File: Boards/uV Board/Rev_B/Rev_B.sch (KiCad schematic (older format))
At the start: 3 parts, among them M2.5 CMH

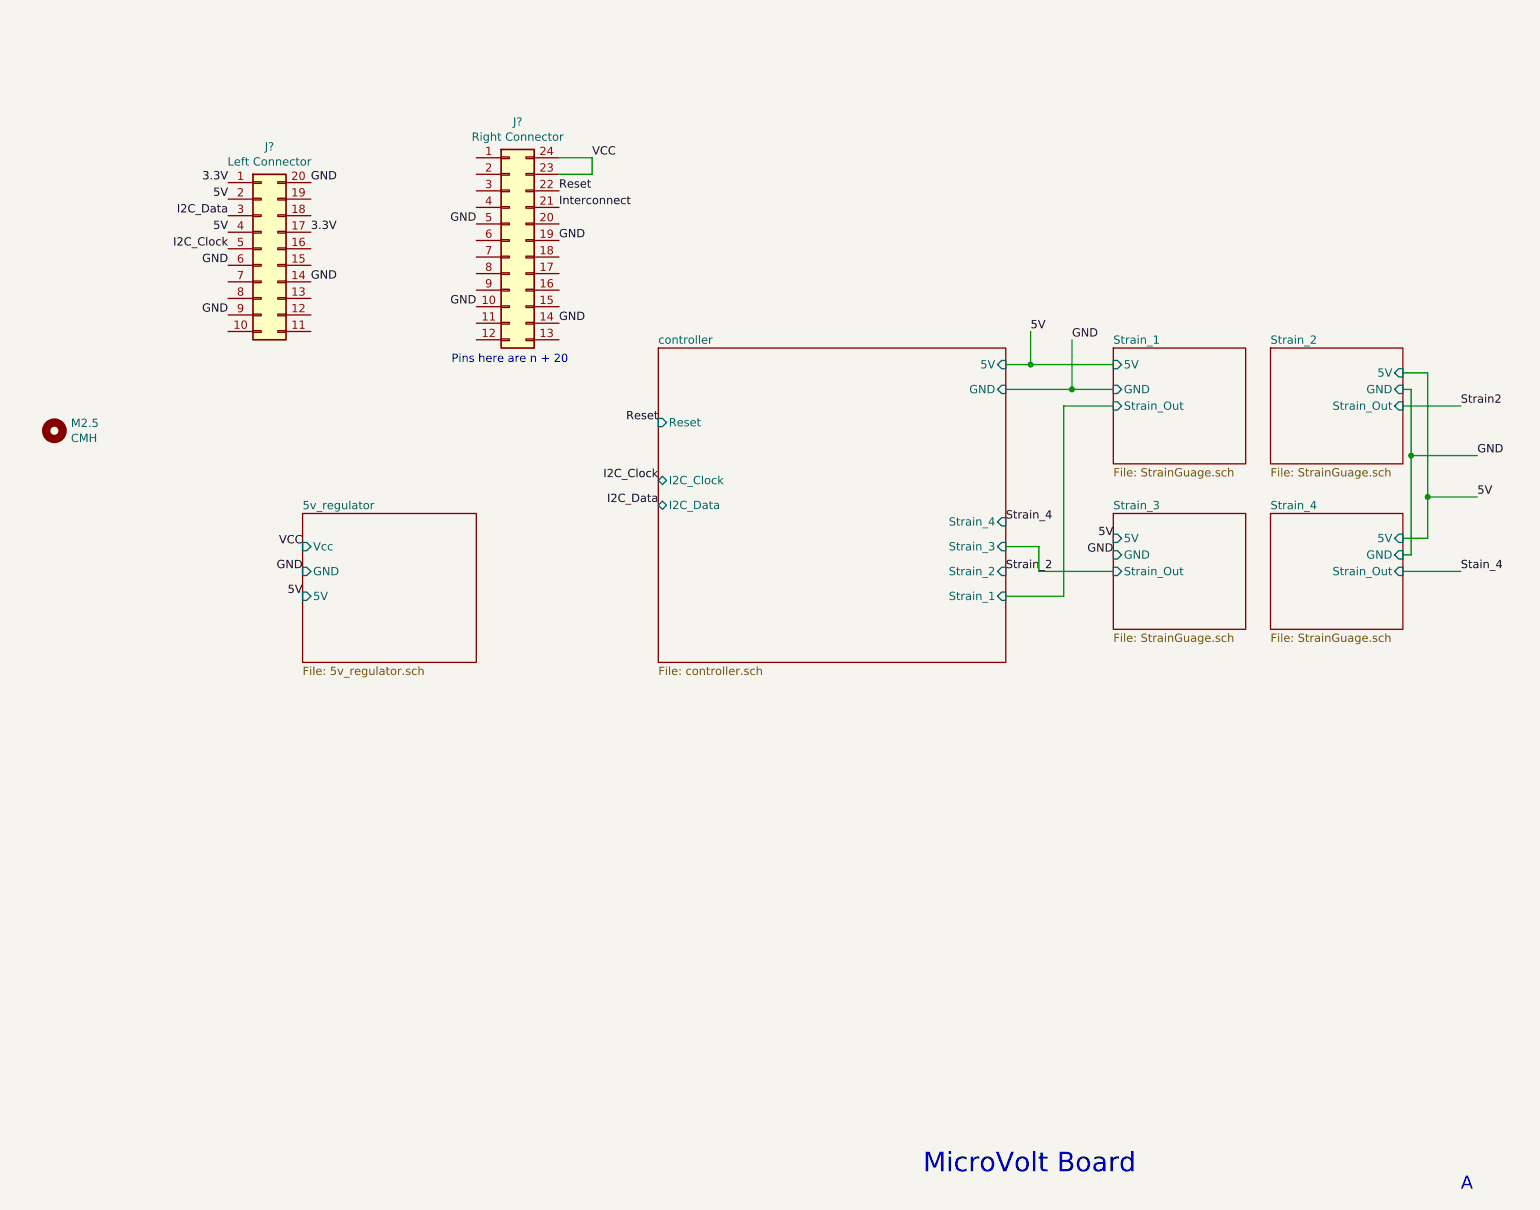
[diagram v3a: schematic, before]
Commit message: Fixed regulator nonsense on ADC board. Rules checked both ADC and micro boards. Fixed interconnect on ADC board.
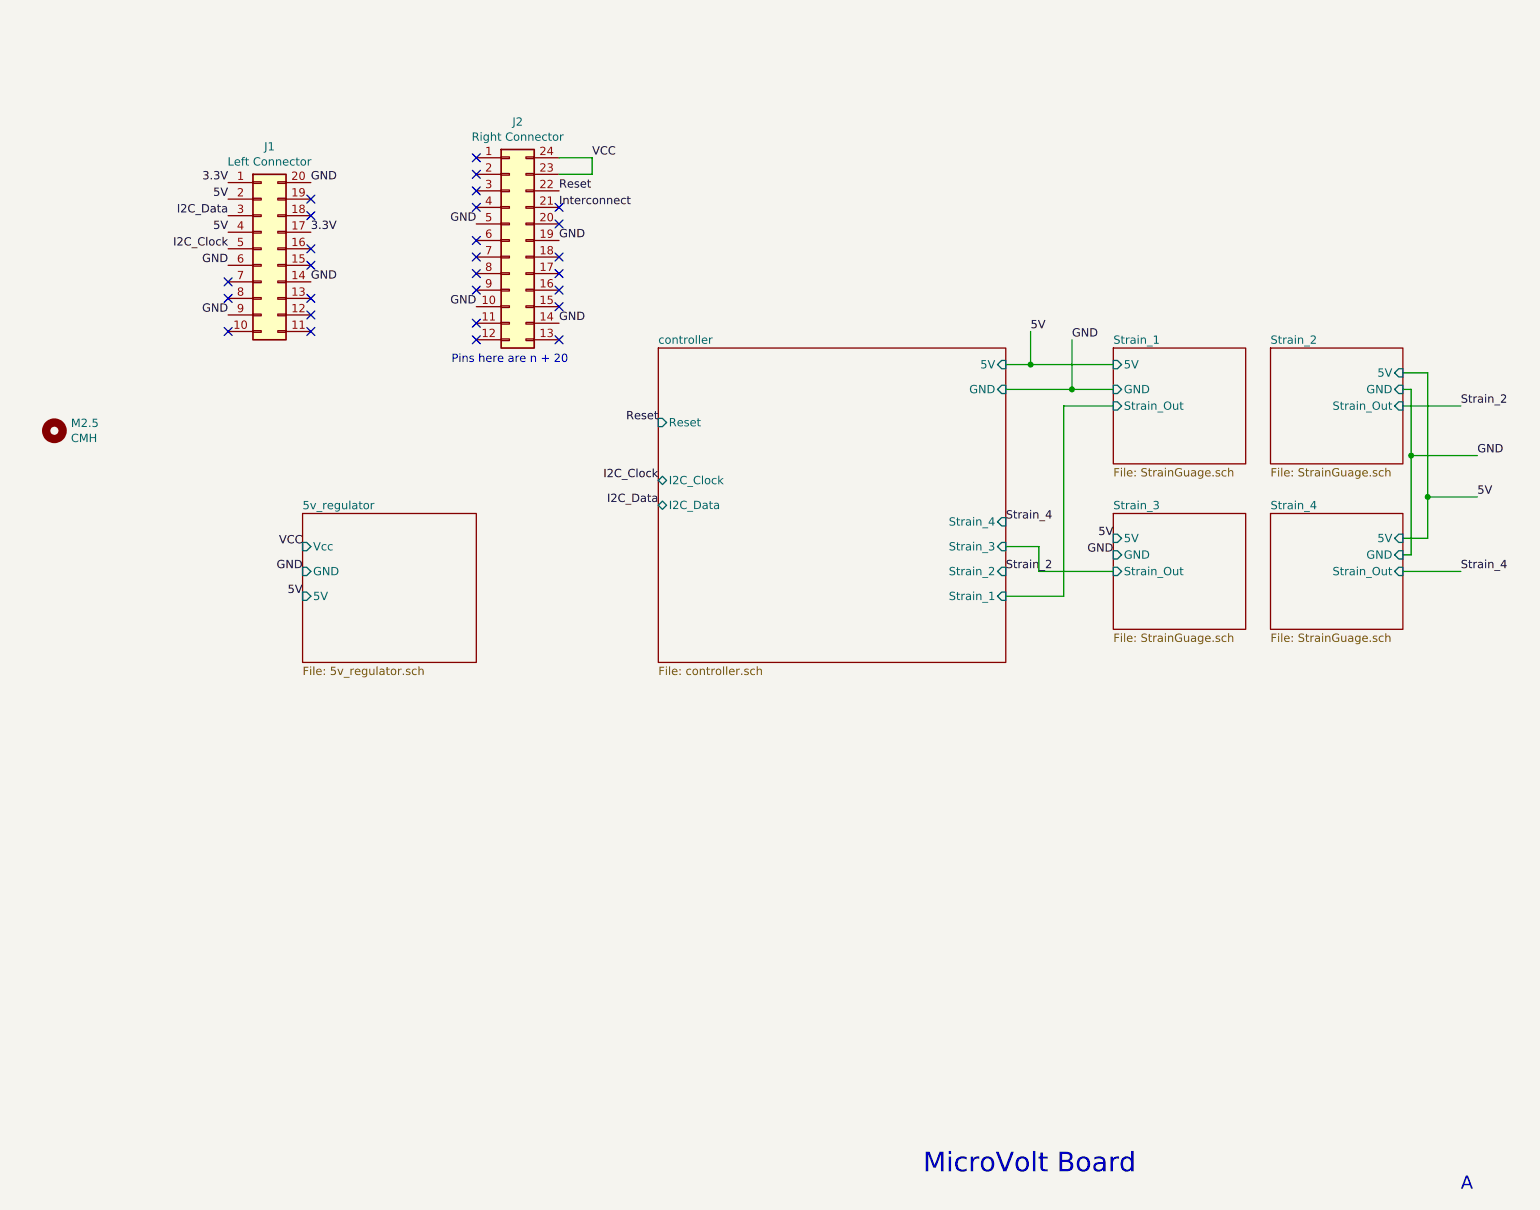
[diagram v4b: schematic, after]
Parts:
- gave numbers to parts that had none: 2
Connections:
- no-connect marks 0 -> 27
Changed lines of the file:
@@
 $EndDescr
 $Comp
-L Connector_Generic:Conn_02x12_Counter_Clockwise J?
+L Connector_Generic:Conn_02x12_Counter_Clockwise J2
 U 1 1 614D23CF
 P 4850 1900
-F 0 "J?" H 4900 2617 50  0000 C CNN
+F 0 "J2" H 4900 2617 50  0000 C CNN
 F 1 "Right Connector" H 4900 2526 50  0000 C CNN
 F 2 "" H 4850 1900 50  0001 C CNN
@@
 GND
 $Comp
-L Connector_Generic:Conn_02x10_Counter_Clockwise J?
+L Connector_Generic:Conn_02x10_Counter_Clockwise J1
 U 1 1 614D9C1F
 P 3350 1950
-F 0 "J?" H 3400 2567 50  0000 C CNN
+F 0 "J1" H 3400 2567 50  0000 C CNN
 F 1 "Left Connector" H 3400 2476 50  0000 C CNN
 F 2 "" H 3350 1950 50  0001 C CNN
@@
 Strain_4
 Text Label 10600 2900 0    50   ~ 0
-Strain2
+Strain_2
 Text Label 10600 3900 0    50   ~ 0
-Stain_4
+Strain_4
 Wire Wire Line
 	10250 2900 10600 2900
@@
 Text Label 3600 3900 2    50   ~ 0
 GND
+NoConn ~ 3150 2150
+NoConn ~ 3150 2250
+NoConn ~ 3150 2450
+NoConn ~ 3650 2450
+NoConn ~ 3650 2350
+NoConn ~ 3650 2250
+NoConn ~ 3650 2050
+NoConn ~ 3650 1950
+NoConn ~ 3650 1750
+NoConn ~ 3650 1650
+NoConn ~ 4650 1400
+NoConn ~ 4650 1500
+NoConn ~ 4650 1600
+NoConn ~ 4650 1700
+NoConn ~ 4650 1900
+NoConn ~ 4650 2000
+NoConn ~ 4650 2100
+NoConn ~ 4650 2200
+NoConn ~ 4650 2400
+NoConn ~ 4650 2500
+NoConn ~ 5150 2500
+NoConn ~ 5150 2300
+NoConn ~ 5150 2200
+NoConn ~ 5150 2100
+NoConn ~ 5150 2000
+NoConn ~ 5150 1800
+NoConn ~ 5150 1700
 $EndSCHEMATC

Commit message: Moved around components on the ADC board PCB. Assigned footprints to microVolt board components.
Tried to add 6-pin spring connector to custom schematics list.
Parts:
- J1: footprint (none) -> Connector_PinHeader_2.54mm:PinHeader_2x10_P2.54mm_Vertical
- J2: footprint (none) -> Connector_PinHeader_2.54mm:PinHeader_2x12_P2.54mm_Vertical
- M2.5: footprint (none) -> MountingHole:MountingHole_2.7mm_M2.5
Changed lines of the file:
@@
 F 0 "J2" H 4900 2617 50  0000 C CNN
 F 1 "Right Connector" H 4900 2526 50  0000 C CNN
-F 2 "" H 4850 1900 50  0001 C CNN
+F 2 "Connector_PinHeader_2.54mm:PinHeader_2x12_P2.54mm_Vertical" H 4850 1900 50  0001 C CNN
 F 3 "~" H 4850 1900 50  0001 C CNN
 	1    4850 1900
@@
 F 0 "J1" H 3400 2567 50  0000 C CNN
 F 1 "Left Connector" H 3400 2476 50  0000 C CNN
-F 2 "" H 3350 1950 50  0001 C CNN
+F 2 "Connector_PinHeader_2.54mm:PinHeader_2x10_P2.54mm_Vertical" H 3350 1950 50  0001 C CNN
 F 3 "~" H 3350 1950 50  0001 C CNN
 	1    3350 1950
@@
 GND
 Wire Wire Line
-	8000 2650 8000 2450
-Wire Wire Line
-	8250 2800 8250 2500
-Wire Wire Line
 	10250 3800 10300 3800
 Wire Wire Line
@@
 Wire Wire Line
 	10300 2800 10250 2800
-Wire Wire Line
-	8500 2900 8200 2900
 Text Label 7850 3900 0    50   ~ 0
 Strain_2
@@
 Wire Wire Line
 	10250 3900 10600 3900
-Wire Wire Line
-	8200 2900 8200 4050
-Wire Wire Line
-	7850 4050 8200 4050
-Wire Wire Line
-	7850 3750 8050 3750
-Wire Wire Line
-	8050 3750 8050 3900
-Wire Wire Line
-	8050 3900 8500 3900
 Text Label 5150 1600 0    50   ~ 0
 Reset
@@
 F4 "Strain_Out" I L 8500 2900 50
 $EndSheet
-Wire Wire Line
-	7850 2650 8000 2650
-Connection ~ 8000 2650
-Wire Wire Line
-	8000 2650 8500 2650
-Connection ~ 8250 2800
-Wire Wire Line
-	8250 2800 8500 2800
-Wire Wire Line
-	7850 2800 8250 2800
-Text Label 8500 3700 2    50   ~ 0
-5V
-Text Label 8500 3800 2    50   ~ 0
-GND
 Text Label 10700 3200 0    50   ~ 0
 GND
@@
 F 0 "M2.5" H 2200 3096 50  0000 L CNN
 F 1 "CMH" H 2200 3005 50  0000 L CNN
-F 2 "" H 2100 3050 50  0001 C CNN
+F 2 "MountingHole:MountingHole_2.7mm_M2.5" H 2100 3050 50  0001 C CNN
 F 3 "~" H 2100 3050 50  0001 C CNN
 	1    2100 3050
@@
 NoConn ~ 5150 1800
 NoConn ~ 5150 1700
+Wire Wire Line
+	8500 3800 8450 3800
+Wire Wire Line
+	8450 3800 8450 2800
+Wire Wire Line
+	8450 2800 8500 2800
+Wire Wire Line
+	8500 3700 8350 3700
+Wire Wire Line
+	8350 3700 8350 2650
+Wire Wire Line
+	8350 2650 8500 2650
+Wire Wire Line
+	7850 2650 8000 2650
+Connection ~ 8350 2650
+Wire Wire Line
+	7850 2800 8250 2800
+Connection ~ 8450 2800
+Wire Wire Line
+	8250 2500 8250 2800
+Connection ~ 8250 2800
+Wire Wire Line
+	8250 2800 8450 2800
+Wire Wire Line
+	8000 2450 8000 2650
+Connection ~ 8000 2650
+Wire Wire Line
+	8000 2650 8350 2650
+Text Label 8350 4300 2    50   ~ 0
+Strain_3
+Text Label 7850 3750 0    50   ~ 0
+Strain_3
+Text Label 8250 2900 2    50   ~ 0
+Strain_1
+Text Label 7850 4050 0    50   ~ 0
+Strain_1
+Wire Wire Line
+	8500 2900 8250 2900
+Wire Wire Line
+	8500 3900 8350 3900
+Wire Wire Line
+	8350 3900 8350 4300
 $EndSCHEMATC

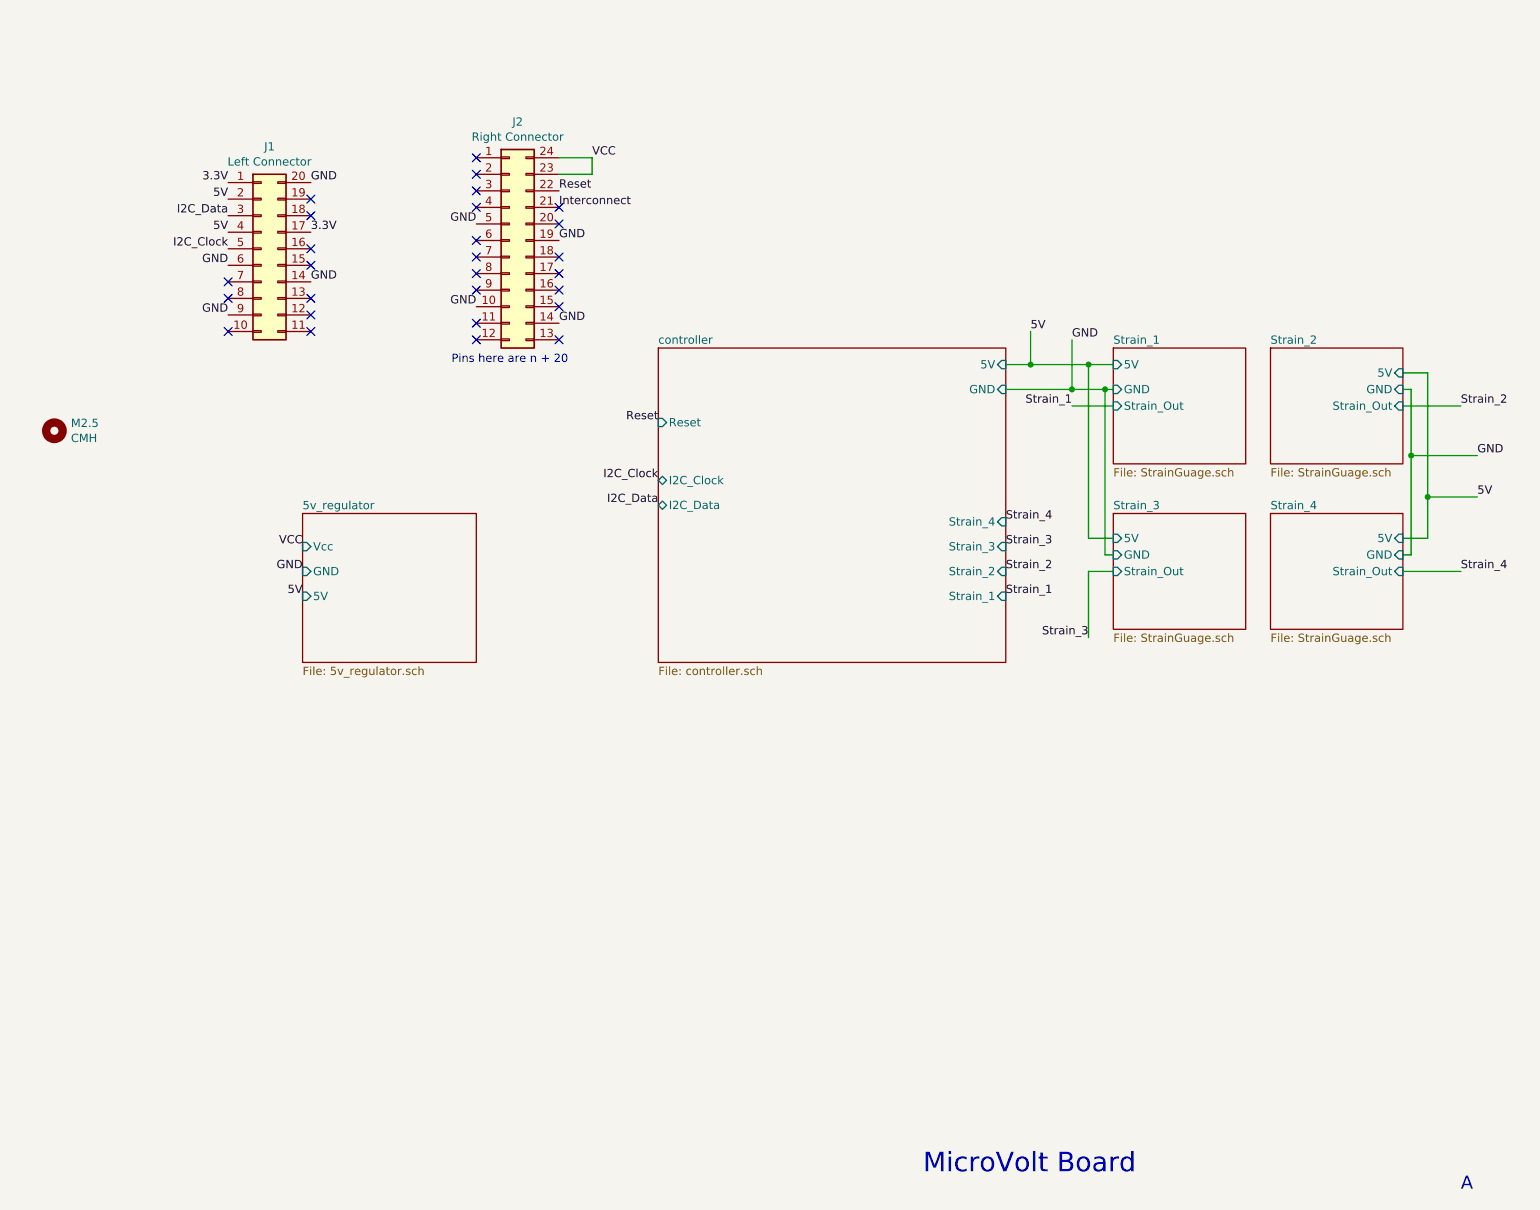
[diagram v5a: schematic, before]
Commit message: Created and layed out most of PCB for microvolt board. Removed one strain module, and added multiple mounting holes for the boards to be placed on.
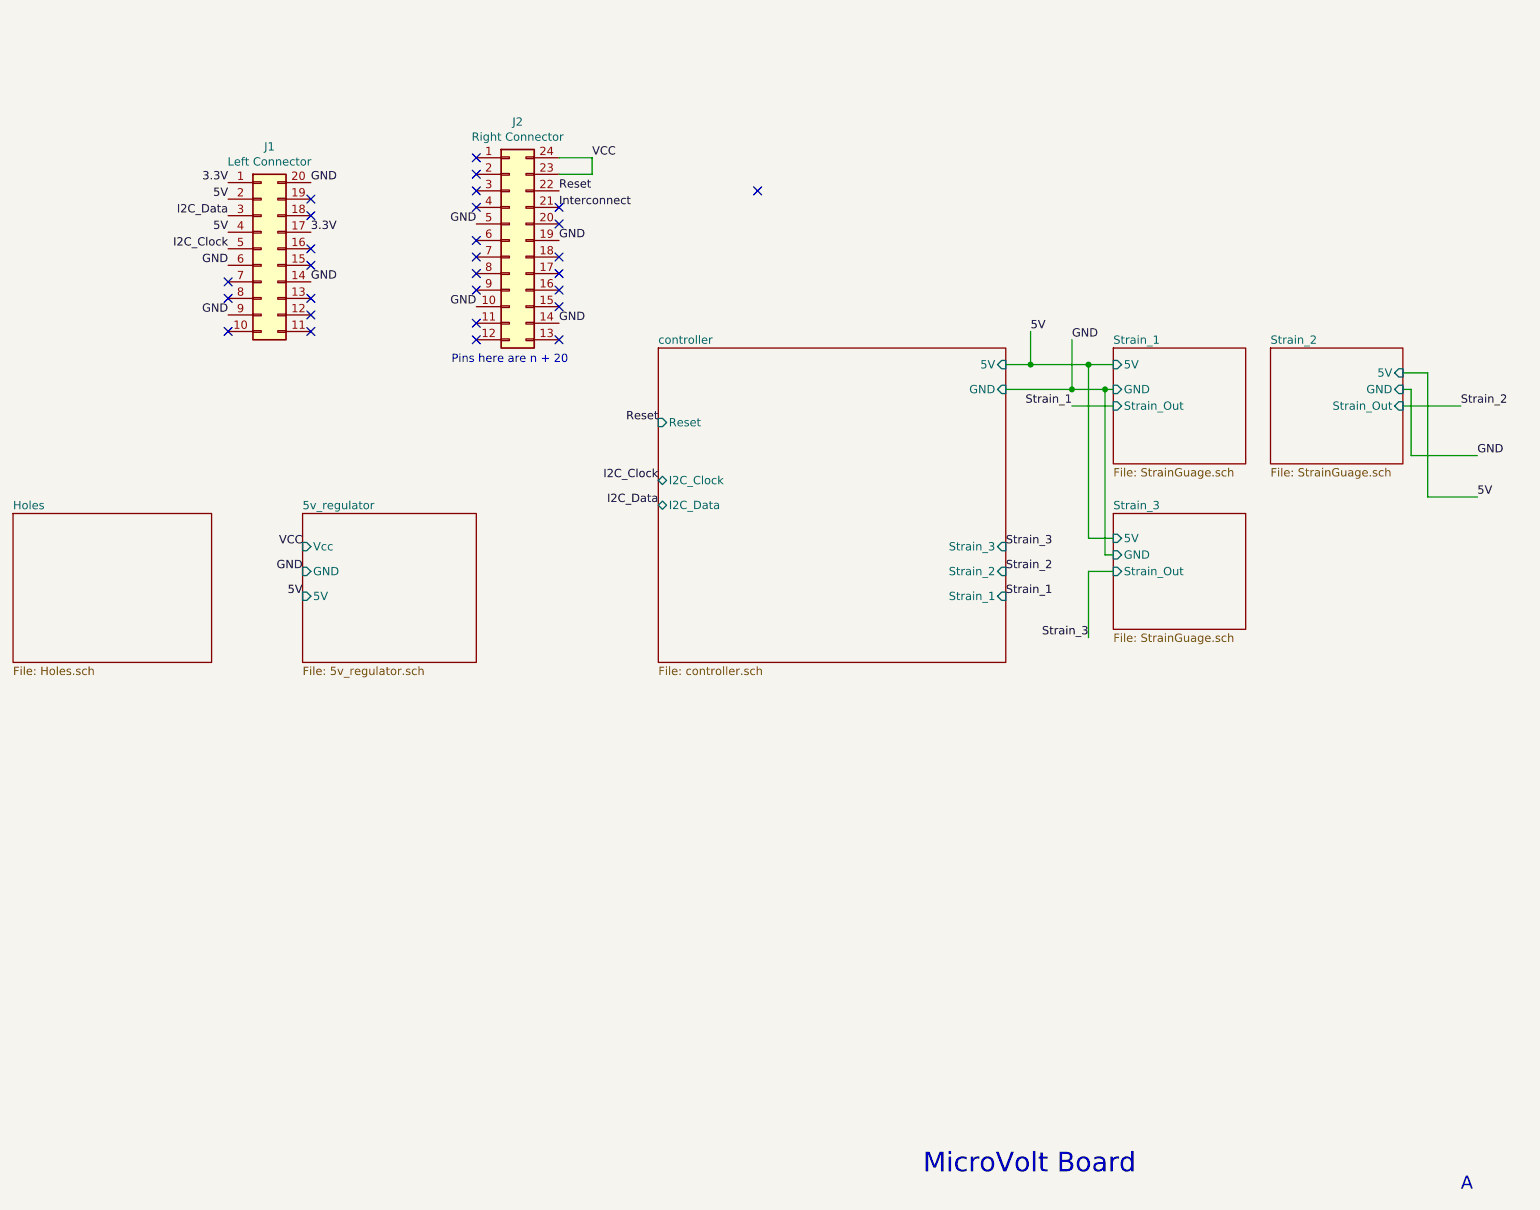
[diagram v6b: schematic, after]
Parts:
- removed M2.5: CMH, MountingHole:MountingHole_2.7mm_M2.5, symbol Mechanical:MountingHole
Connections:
- no-connect marks 27 -> 28
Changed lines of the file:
@@
 F3 "5V" I R 7850 2650 50
 F4 "Reset" I L 5750 3000 50
-F5 "Strain_4" I R 7850 3600 50
-F6 "Strain_3" I R 7850 3750 50
-F7 "Strain_2" I R 7850 3900 50
-F8 "Strain_1" I R 7850 4050 50
-F9 "I2C_Clock" B L 5750 3350 50
-F10 "I2C_Data" B L 5750 3500 50
+F5 "Strain_3" I R 7850 3750 50
+F6 "Strain_2" I R 7850 3900 50
+F7 "Strain_1" I R 7850 4050 50
+F8 "I2C_Clock" B L 5750 3350 50
+F9 "I2C_Data" B L 5750 3500 50
 $EndSheet
 Text Notes 4500 2650 0    50   ~ 0
@@
 F4 "Strain_Out" I L 8500 3900 50
 $EndSheet
-$Sheet
-S 9450 3550 800  700
-U 61575905
-F0 "Strain_4" 50
-F1 "StrainGuage.sch" 50
-F2 "5V" I R 10250 3700 50
-F3 "GND" I R 10250 3800 50
-F4 "Strain_Out" I R 10250 3900 50
-$EndSheet
 Wire Wire Line
 	10250 2700 10400 2700
 Wire Wire Line
 	10400 2700 10400 3450
-Wire Wire Line
-	10400 3700 10250 3700
 Text Label 8000 2450 0    50   ~ 0
 5V
@@
 GND
 Wire Wire Line
-	10250 3800 10300 3800
-Wire Wire Line
-	10300 3800 10300 3200
-Wire Wire Line
 	10300 2800 10250 2800
 Text Label 7850 3900 0    50   ~ 0
 Strain_2
-Text Label 7850 3600 0    50   ~ 0
-Strain_4
 Text Label 10600 2900 0    50   ~ 0
 Strain_2
-Text Label 10600 3900 0    50   ~ 0
-Strain_4
 Wire Wire Line
 	10250 2900 10600 2900
-Wire Wire Line
-	10250 3900 10600 3900
 Text Label 5150 1600 0    50   ~ 0
 Reset
@@
 Wire Wire Line
 	10700 3200 10300 3200
-Connection ~ 10300 3200
 Wire Wire Line
 	10300 3200 10300 2800
 Wire Wire Line
 	10700 3450 10400 3450
-Connection ~ 10400 3450
-Wire Wire Line
-	10400 3450 10400 3700
 Text Label 3150 1950 2    50   ~ 0
 I2C_Clock
@@
 Text Label 5150 1700 0    50   ~ 0
 Interconnect
-$Comp
-L Mechanical:MountingHole M2.5
-U 1 1 615FF776
-P 2100 3050
-F 0 "M2.5" H 2200 3096 50  0000 L CNN
-F 1 "CMH" H 2200 3005 50  0000 L CNN
-F 2 "MountingHole:MountingHole_2.7mm_M2.5" H 2100 3050 50  0001 C CNN
-F 3 "~" H 2100 3050 50  0001 C CNN
-	1    2100 3050
-	1    0    0    -1
-$EndComp
 $Sheet
 S 3600 3550 1050 900
@@
 Wire Wire Line
 	8350 3900 8350 4300
+NoConn ~ 6350 1600
+$Sheet
+S 1850 3550 1200 900
+U 61F58F90
+F0 "Holes" 50
+F1 "Holes.sch" 50
+$EndSheet
 $EndSCHEMATC
